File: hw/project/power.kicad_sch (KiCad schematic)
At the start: 27 parts, among them Q1 MOSFET, N-CH, SINGLE, 120A, 6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, Q2 MOSFET, N-CH, SINGLE, 120A, 6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, U3 LM74502DDFR, U4 LMR51610XDBVR

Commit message: Prep to revamp power sheet
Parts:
- removed R55: 10k, symbol Device:R_Small_US
- added R105: 10k, Resistor_SMD:R_0603_1608Metric, symbol Device:R_Small_US
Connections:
- net PGND: now also R105.2
- net at C48.1, R54.2, U3.1 (EN_UVLO): now also R105.1
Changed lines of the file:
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@@
-	)
-	(symbol
-		(lib_id "Device:R_Small_US")
-		(at 125.73 62.23 0)
-		(unit 1)
-		(body_style 1)
-		(exclude_from_sim no)
-		(in_bom yes)
-		(on_board yes)
-		(in_pos_files yes)
-		(dnp no)
-		(fields_autoplaced yes)
-		(property "Reference" "R55"
-			(at 128.27 60.9599 0)
-			(show_name no)
-			(do_not_autoplace no)
-			(effects
-				(font
-					(size 1.27 1.27)
-				)
-				(justify left)
-			)
-		)
-		(property "Value" "10k"
-			(at 128.27 63.4999 0)
-			(show_name no)
-			(do_not_autoplace no)
-			(effects
-				(font
-					(size 1.27 1.27)
-				)
-				(justify left)
-			)
-		)
-		(property "Footprint" ""
-			(at 125.73 62.23 0)
-			(hide yes)
-			(show_name no)
-			(do_not_autoplace no)
-			(effects
-				(font
-					(size 1.27 1.27)
-				)
-			)
-		)
-		(property "Datasheet" ""
-			(at 125.73 62.23 0)
-			(hide yes)
-			(show_name no)
-			(do_not_autoplace no)
-			(effects
-				(font
-					(size 1.27 1.27)
-				)
-			)
-		)
-		(property "Description" ""
-			(at 125.73 62.23 0)
-			(hide yes)
-			(show_name no)
-			(do_not_autoplace no)
-			(effects
-				(font
-					(size 1.27 1.27)
-				)
-			)
-		)
-		(pin "1"
-		)
-		(pin "2"
-		)
-		(instances
-			(project "esc"
-				(path "/86a17c4d-db96-42a1-af84-d43fe593f4e6/5338eeb3-4021-4459-b70f-dab93d7c7a1a"
-					(reference "R55")
-					(unit 1)
-				)
-			)
-		)
 	)
 	(symbol
@@
 					(unit 1)
 				)
+			)
+		)
+	)
+	(symbol
+		(lib_id "Device:R_Small_US")
+		(at 125.73 62.23 0)
+		(unit 1)
+		(body_style 1)
+		(exclude_from_sim no)
+		(in_bom yes)
+		(on_board yes)
+		(in_pos_files yes)
+		(dnp no)
+		(fields_autoplaced yes)
+		(property "Reference" "R105"
+			(at 128.27 60.9599 0)
+			(show_name no)
+			(do_not_autoplace no)
+			(effects
+				(font
+					(size 1.27 1.27)
+				)
+				(justify left)
+			)
+		)
+		(property "Value" "10k"
+			(at 128.27 63.4999 0)
+			(show_name no)
+			(do_not_autoplace no)
+			(effects
+				(font
+					(size 1.27 1.27)
+				)
+				(justify left)
+			)
+		)
+		(property "Footprint" "Resistor_SMD:R_0603_1608Metric"
+			(at 125.73 62.23 0)
+			(hide yes)
+			(show_name no)
+			(do_not_autoplace no)
+			(effects
+				(font
+					(size 1.27 1.27)
+				)
+			)
+		)
+		(property "Datasheet" "https://www.digikey.ca/en/products/detail/yageo/RC0603FR-0710KL/726880"
+			(at 125.73 62.23 0)
+			(hide yes)
+			(show_name no)
+			(do_not_autoplace no)
+			(effects
+				(font
+					(size 1.27 1.27)
+				)
+			)
+		)
+		(property "Description" "RES 10K OHM 1% 1/10W 0603"
+			(at 125.73 62.23 0)
+			(hide yes)
+			(show_name no)
+			(do_not_autoplace no)
+			(effects
+				(font
+					(size 1.27 1.27)
+				)
+			)
+		)
+		(pin "1"
+		)
+		(pin "2"
+		)
+		(instances
+			(project "esc"
+				(path "/86a17c4d-db96-42a1-af84-d43fe593f4e6/5338eeb3-4021-4459-b70f-dab93d7c7a1a"
+					(reference "R105")
+					(unit 1)
+				)

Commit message: Continuing power revamp tomorrow
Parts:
- removed C20: 0.1uF, Capacitor_SMD:C_0603_1608Metric, symbol Device:C_Small
- removed C22: 220nF, Capacitor_SMD:C_0603_1608Metric, symbol Device:C_Small
- removed C25: 27nF, Capacitor_SMD:C_0603_1608Metric, symbol Device:C_Small
- removed C27, C28, C29, C30: 68uF, 100ZLH68MEFC8X20:CAP_YX_8X20_RUB, symbol Device:C_Small_US
- removed C31: 18uF, 100ZLH18MEFC6_3X11:CAP_YX_6P3X11_RUB, symbol Device:C_Small_US
- removed C48: 100nF, symbol Device:C_Small_US
- removed D14: TVS DIODE 60VWM 96.8VC DO214AB, Diode_SMD:D_SMC, symbol Diode:SM15T36A
- removed Q1, Q2: MOSFET, N-CH, SINGLE, 120A, 65V,, GSFP06120:GSFP06120, symbol GSFP06120:GSFP06120
- removed R15: 49.9k, Resistor_SMD:R_0603_1608Metric, symbol Device:R_Small_US
- removed R16: 1070, Resistor_SMD:R_0603_1608Metric, symbol Device:R_Small_US
- removed R19: 50, Resistor_SMD:R_0603_1608Metric, symbol Device:R_Small_US
- removed R54: 21.5k, symbol Device:R_Small_US
- removed U3: LM74502DDFR, LM74502DDFR:LM74502DDFR-MFG, symbol LM74502DDFR:LM74502DDFR
- added D3: D_Zener, symbol Device:D_Zener
- added Q1, Q2, Q3, Q4: GT090P08M, Package_TO_SOT_SMD:TO-263-2, symbol Transistor_FET:Q_PMOS_GDS
- added R1: 100k/0.25W OR 0.5W? check, symbol Device:R_Small_US
- added R103, R108, R109: 10, Resistor_SMD:R_0603_1608Metric, symbol Device:R_Small_US
- R105: value 10k -> 10
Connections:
- net PGND: no longer R105.2
- net VM_IN: now also Q1.2 (D), Q2.2 (D), Q3.2 (D), Q4.2 (D)
- net at R105.1: now also Q2.1 (G)
- new net: Q1.1 (G), R103.1
- new net: D3.2 (A), R1.1, R103.2, R105.2, R108.2, R109.2
- new net: Q3.1 (G), R108.1
- new net: Q4.1 (G), R109.1
- new net PGND?: R1.2
- new net VM_RPP: D3.1 (K), Q1.3 (S), Q2.3 (S), Q3.3 (S), Q4.3 (S)
- no-connect marks 1 -> 0
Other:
- note added: "1) INPUT CONNECTORS (relocate? probably) 2) TVS Diode 3) RPP (done, just need to hookup) 4) Cap Bank and Inductor"
- note added: "calculate junction tempearture"
- note added: "change power source"
- note added: "remove?"
- note removed: "OV voltage picked to be triggered at 60V"
- note removed: "Rds = 3.5m @ 30a P = 30^2(3.5m) = 3.15w"
- note removed: "Reverse Polarity & Soft Start"
- note removed: "starts up SiP above 5.5V min"
- moved on the sheet: C18, C21, C24, C26, L2, R17, R18, TP2, U4

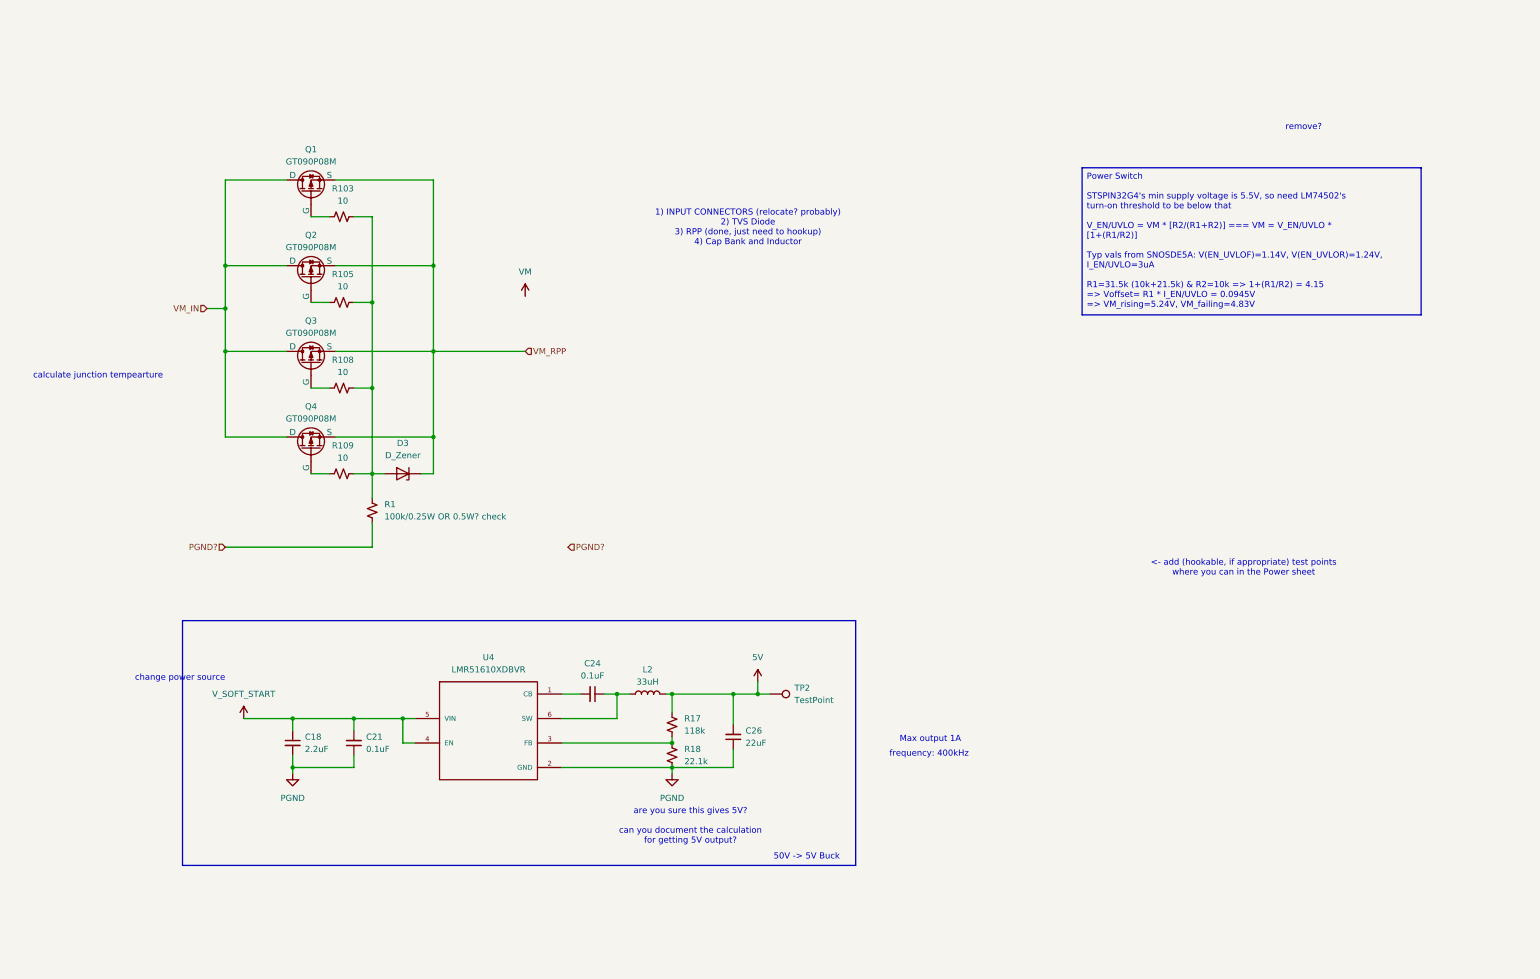
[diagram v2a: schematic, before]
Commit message: First draft of power revamp
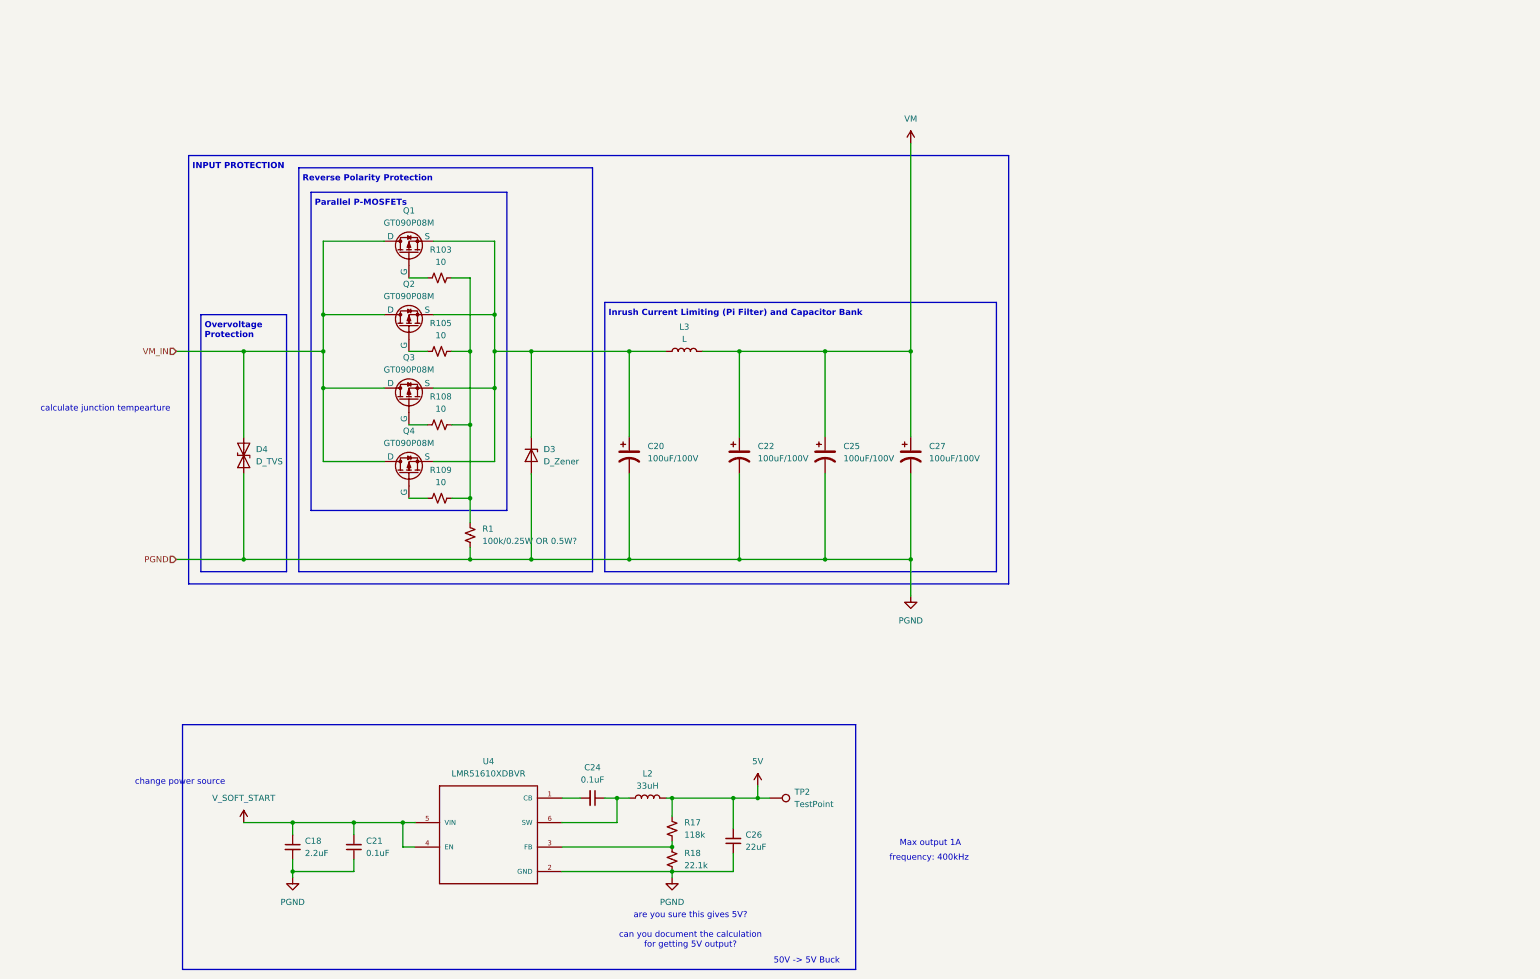
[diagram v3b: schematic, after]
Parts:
- added C20, C22, C25, C27: 100uF/100V, symbol Device:C_Polarized_US
- added D4: D_TVS, symbol Device:D_TVS
- added L3: L, symbol Device:L
- R1: value 100k/0.25W OR 0.5W? check -> 100k/0.25W OR 0.5W?
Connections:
- net PGND? is gone; now on net PGND: R1.2
- net PGND: now also D3.2 (A), C20.2, C22.2, C25.2, C27.2, D4.1 (A1)
- net VM: now also C22.1, C25.1, C27.1, L3.2
- net VM_IN: now also D4.2 (A2)
- net at R1.1, R103.2, R105.2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: no longer D3.2 (A)
- net VM_RPP: no longer names the net of D3.1 (K), Q1.3 (S), Q2.3 (S), Q3.3 (S), Q4.3 (S)
- net VM_RPP: now also C20.1, L3.1
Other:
- note added: "INPUT PROTECTION"
- note added: "Inrush Current Limiting (Pi Filter) and Capacitor Bank"
- note added: "Overvoltage Protection"
- note added: "Parallel P-MOSFETs"
- note added: "Reverse Polarity Protection"
- note removed: "1) INPUT CONNECTORS (relocate? probably) 2) TVS Diode 3) RPP (done, just need to hookup) 4) Cap Bank and Inductor"
- note removed: "<- add (hookable, if appropriate) test points where you can in the Power sheet"
- note removed: "remove?"
- moved on the sheet: C18, C21, C24, C26, D3, L2, Q1, Q2, Q3, Q4, R1, R103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

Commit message: Checkpoint: Undid precharge circuit with diode, resistor, and delay cap
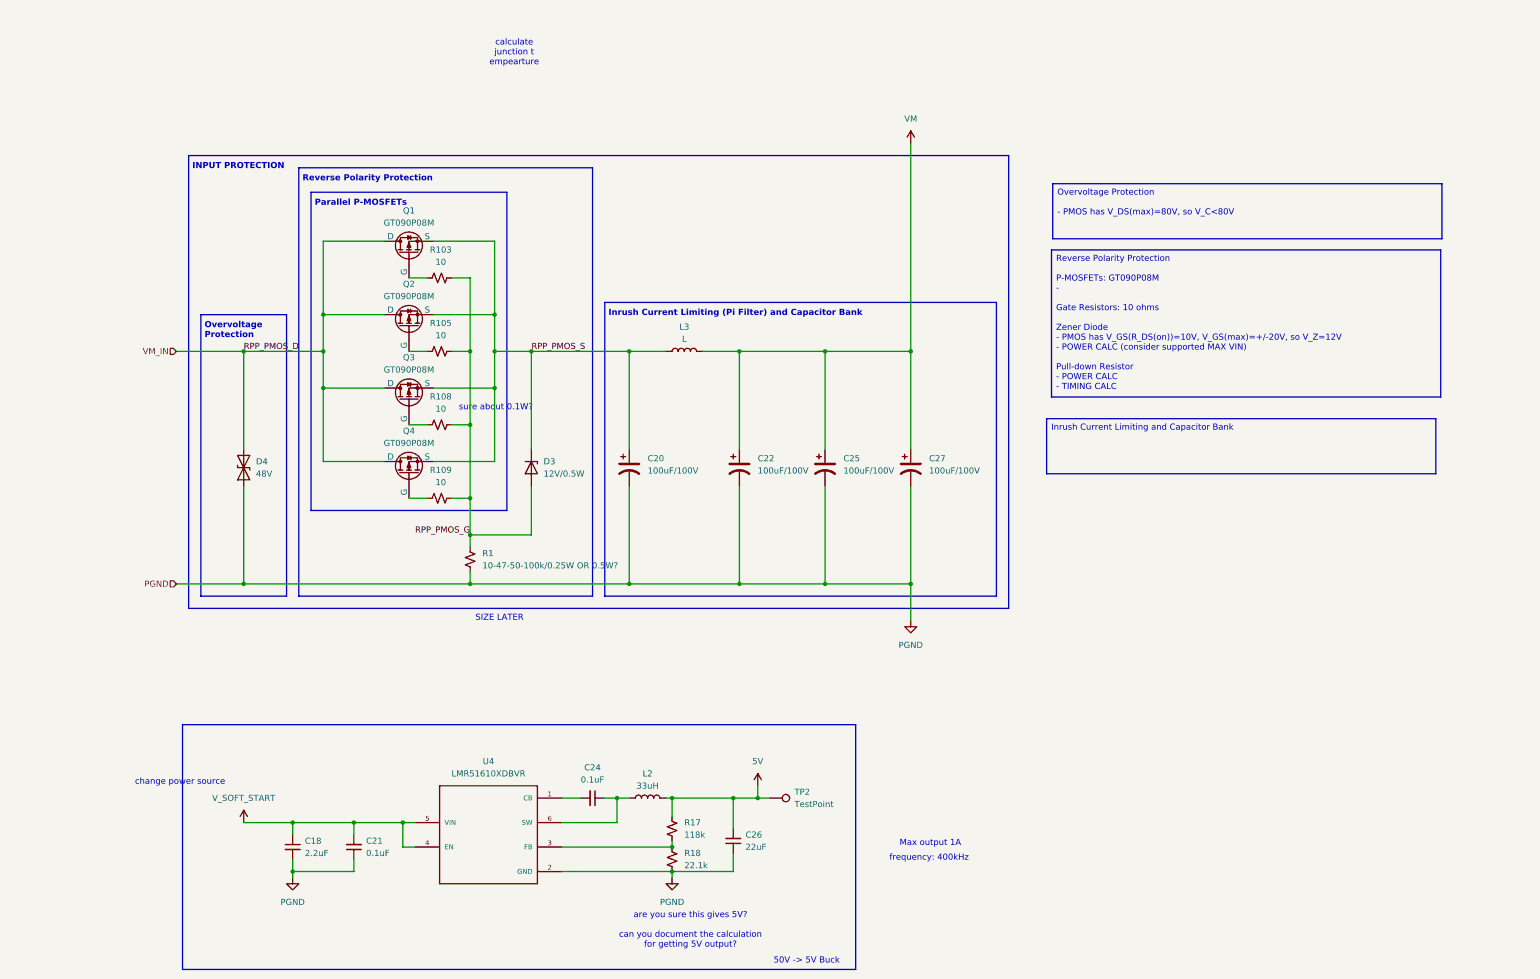
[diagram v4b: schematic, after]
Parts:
- D3: value D_Zener -> 12V/0.5W; footprint (none) -> Diode_SMD:D_SOD-123
- D4: value D_TVS -> 48V
- R1: value 100k/0.25W OR 0.5W? -> 10-47-50-100k/0.25W OR 0.5W?
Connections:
- net PGND: no longer D3.2 (A)
- net RPP_PMOS_G: now reaches R1.1, R103.2, R105.2, R108.2, R109.2
- net RPP_PMOS_G: now also D3.2 (A)
- net RPP_PMOS_S: now reaches C20.1, D3.1 (K), L3.1, Q1.3 (S), Q2.3 (S), Q3.3 (S), Q4.3 (S)
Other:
- note added: "SIZE LATER"
- note added: "calculate junction t empearture"
- note added: "sure about 0.1W?"
- note removed: "calculate junction tempearture"
- moved on the sheet: C20, C22, C25, C27, D3, D4, R1

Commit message: Checkpoint: Ready to spec rest of power stage tom
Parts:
- removed C20: 100uF/100V, symbol Device:C_Polarized_US
- removed L3: L, symbol Device:L
- removed Q3, Q4: GT090P08M, Package_TO_SOT_SMD:TO-263-2, symbol Transistor_FET:Q_PMOS_GDS
- removed R103, R105, R108, R109: 10, Resistor_SMD:R_0603_1608Metric, symbol Device:R_Small_US
- added C43: 220nF, Capacitor_SMD:C_0603_1608Metric, symbol Device:C_Small
- added D14: 12V, Diode_SMD:D_SOD-123, symbol Device:D_Zener
- added R19: 22.1k, Resistor_SMD:R_0603_1608Metric, symbol Device:R_Small_US
- added R2: 100k, symbol Device:R_Small_US
- C22, C25, C27: value 100uF/100V -> 220uF/63V
- D3: value 12V/0.5W -> 12V
- D4: value 48V -> 47.8V
- Q1, Q2: value GT090P08M -> SQM50061EL_GE3
- R1: value 10-47-50-100k/0.25W OR 0.5W? -> 100k
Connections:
- net RPP_PMOS_G is gone; now on an unnamed net: D3.2 (A), R1.1
- net PGND: now also R19.2, R2.2
- net VM: now also Q2.2 (D), R19.1
- net VM_IN: no longer Q2.2 (D)
- net at Q2.1 (G): now also C43.1, D14.2 (A), R2.1
- net RPP_PMOS_S: no longer names the net of D3.1 (K), Q1.3 (S), Q2.3 (S)
- net RPP_PMOS_S: now also C43.2, D14.1 (K)
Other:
- note added: "1) Spec rest of this page, then write notes 2) Confirm 5V 3) verify with claude about drive sheet 4) deal with 22k vs 22.1k 5) DRC check"
- note added: "Capacitor Bank"
- note added: "Inrush Current Limiting"
- note removed: "Inrush Current Limiting (Pi Filter) and Capacitor Bank"
- note removed: "Parallel P-MOSFETs"
- note removed: "SIZE LATER"
- note removed: "sure about 0.1W?"
- moved on the sheet: C22, C25, C27, D3, D4, Q1, R1

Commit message: Spec bulk caps
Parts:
- removed C25, C27: 220uF/63V, symbol Device:C_Polarized_US
- removed R1, R2: 100k, symbol Device:R_Small_US
- added C25, C27: 430uF/100V, Capacitor_THT:CP_Radial_D12.5mm_P5.00mm, symbol Device:C_Polarized_Small_US
- added R20: 118k, Resistor_SMD:R_0603_1608Metric, symbol Device:R_Small_US
- added R21, R22: 22.1k, Resistor_SMD:R_0603_1608Metric, symbol Device:R_Small_US
- C22: value 220uF/63V -> 430uF/100V; footprint (none) -> Capacitor_THT:CP_Radial_D12.5mm_P5.00mm; symbol Device:C_Polarized_US -> Device:C_Polarized_Small_US
- R19: value 22.1k -> 10k
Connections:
- net PGND: now also C25.2, C27.2, R20.2, R22.2
- net VM: now also C25.1, C27.1, R21.1; no longer R19.1
- net at C43.1, D14.2 (A), Q2.1 (G): now also R20.1
- net at D3.2 (A), Q1.1 (G): now also R19.1
- new net: R21.2, R22.1
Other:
- note added: "Bulk (Electrolytic) Capacitor Bank"
- note added: "reuse in drive stage"
- note added: "spec"
- note removed: "Capacitor Bank"
